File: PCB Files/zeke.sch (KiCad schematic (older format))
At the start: 134 parts, among them J1 USB_C, SW1 MXSwitch, SW10 MXSwitch, SW11 MXSwitch, SW12 MXSwitch, SW13 MXSwitch, SW14 MXSwitch, SW15 MXSwitch, SW16 MXSwitch, SW17 MXSwitch, SW18 MXSwitch, SW19 MXSwitch, SW2 MXSwitch, SW20 MXSwitch, SW21 MXSwitch, SW22 MXSwitch, SW23 MXSwitch, SW24 MXSwitch, SW25 MXSwitch, SW26 MXSwitch, SW27 MXSwitch, SW3 MXSwitch, SW4 MXSwitch, SW5 MXSwitch, SW6 MXSwitch, SW7 MXSwitch, SW8 MXSwitch, SW9 MXSwitch, U1 WS2811M, U10 WS2811M, U11 WS2811M, U12 WS2811M, U13 WS2811M, U14 WS2811M, U15 WS2811M, U16 WS2811M, U17 WS2811M, U18 WS2811M, U19 WS2811M, U2 WS2811M, U20 WS2811M, U21 WS2811M, U22 WS2811M, U23 WS2811M, U24 WS2811M, U28 USBLC6-2SC6, U29 ATMEGA32U4, U3 WS2811M, U4 WS2811M, U5 WS2811M, U6 WS2811M, U7 WS2811M, U8 WS2811M, U9 WS2811M, X1 16MHz

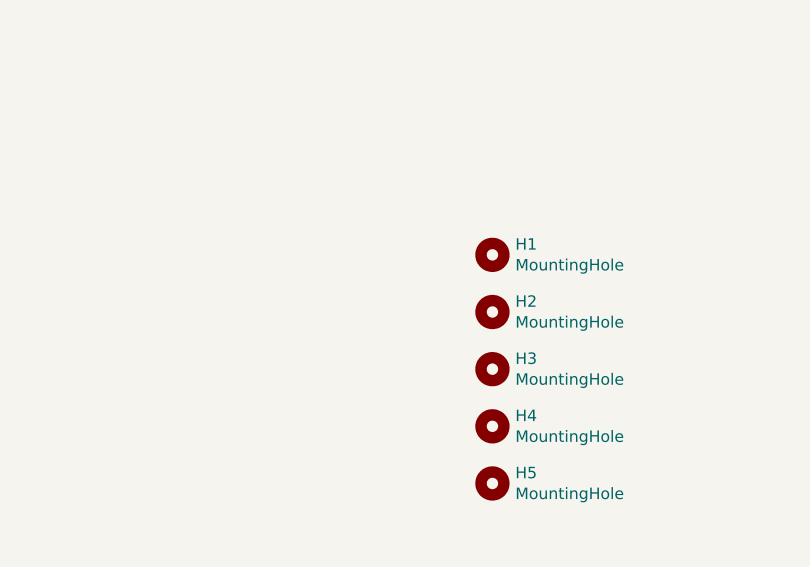
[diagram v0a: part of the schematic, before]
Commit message: [Update] Added new footprint for the RGB LEDs with the 3D model, added Acheron Short logo
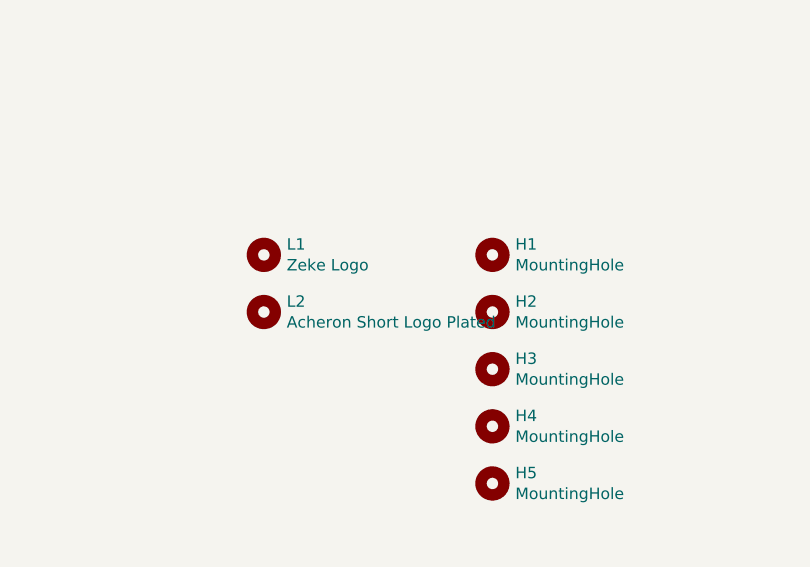
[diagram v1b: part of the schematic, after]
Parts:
- added L1: Zeke Logo, zekeGraphics:zekeLogo, symbol Mechanical:MountingHole
- added L2: Acheron Short Logo Plated, acheron_Logos:acheronShort_0.3x0.5in_Plated, symbol Mechanical:MountingHole
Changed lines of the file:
@@
+	1    0    0    -1
+$EndComp
+$Comp
+L Mechanical:MountingHole L1
+U 1 1 5D47814B
+P 3500 12250
+F 0 "L1" H 3600 12296 50  0000 L CNN
+F 1 "Zeke Logo" H 3600 12205 50  0000 L CNN
+F 2 "zekeGraphics:zekeLogo" H 3500 12250 50  0001 C CNN
+F 3 "~" H 3500 12250 50  0001 C CNN
+	1    3500 12250
+	1    0    0    -1
+$EndComp
+$Comp
+L Mechanical:MountingHole L2
+U 1 1 5D4788D8
+P 3500 12500
+F 0 "L2" H 3600 12546 50  0000 L CNN
+F 1 "Acheron Short Logo Plated" H 3600 12455 50  0000 L CNN
+F 2 "acheron_Logos:acheronShort_0.3x0.5in_Plated" H 3500 12500 50  0001 C CNN
+F 3 "~" H 3500 12500 50  0001 C CNN
+	1    3500 12500
 	1    0    0    -1
 $EndComp
